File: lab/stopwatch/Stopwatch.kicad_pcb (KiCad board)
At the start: 2 copper layers, 90 x 90 mm, 8 parts, among them U1 atmega328p

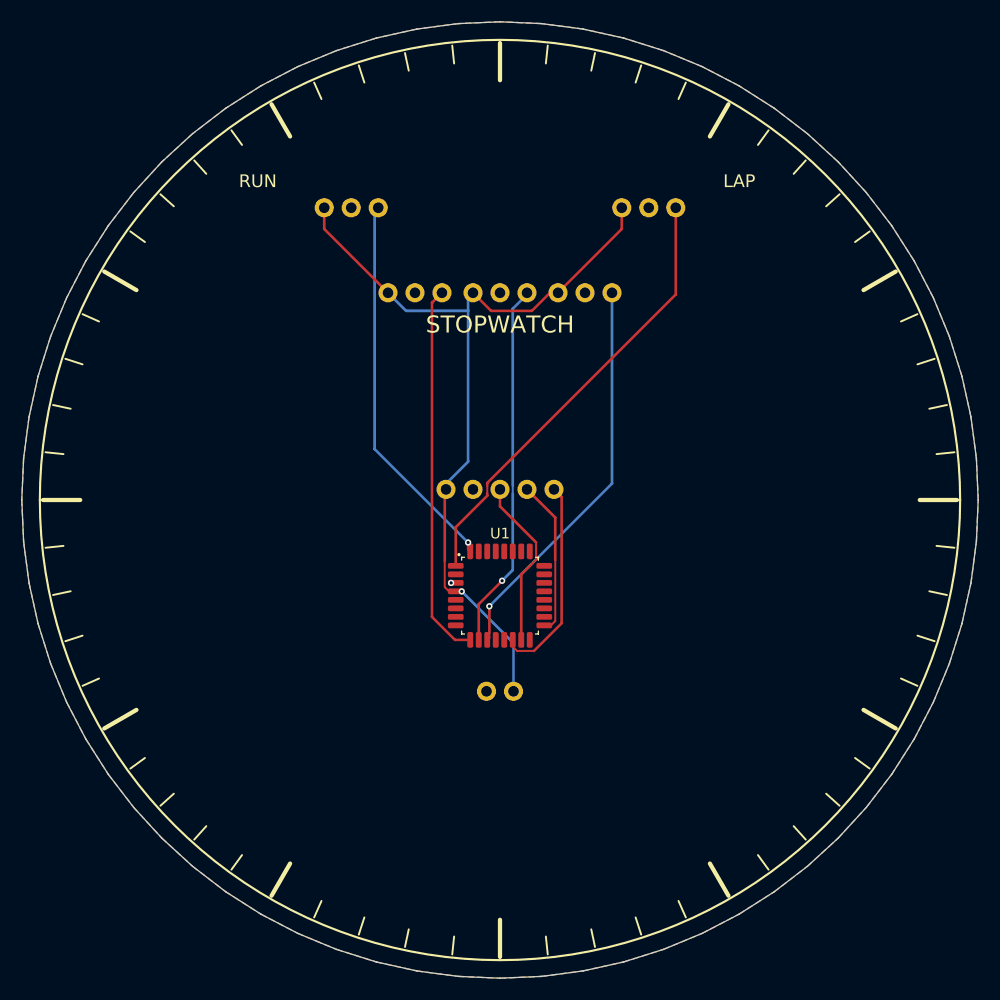
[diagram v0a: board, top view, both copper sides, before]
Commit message: lab: every board is a real board: an Arduino Nano and registry parts, routed, ready to order
The lab boards ran on simulation-only envelopes (labMcu, labDisplay, a battery). Now each is
an Arduino Nano on two sockets on the back (flashed over its USB, the image the app builds),
its lights LEDs through 1 kΩ, its knobs PTV09A pots, its display the MAX7219 eight-digit
module, its sensors an SHT31 and an SCD40 with their datasheets' support circuits, the FTDI
header for the serial console; the servo boards take 5 V on a screw terminal with a bulk
capacitor. All ten check complete with no errors or warnings, their firmware unchanged
(serial-device now on the 328P), and run in the lab without a fault (3 s each, dev host).

The registry: every interactive board must be ready to order and flash (publish.mjs refuses
one that is not; status simulation-only removed).

Claude-Session: https://claude.ai/code/session_01ATmMmxyrWxFwR3nTdXUrcx
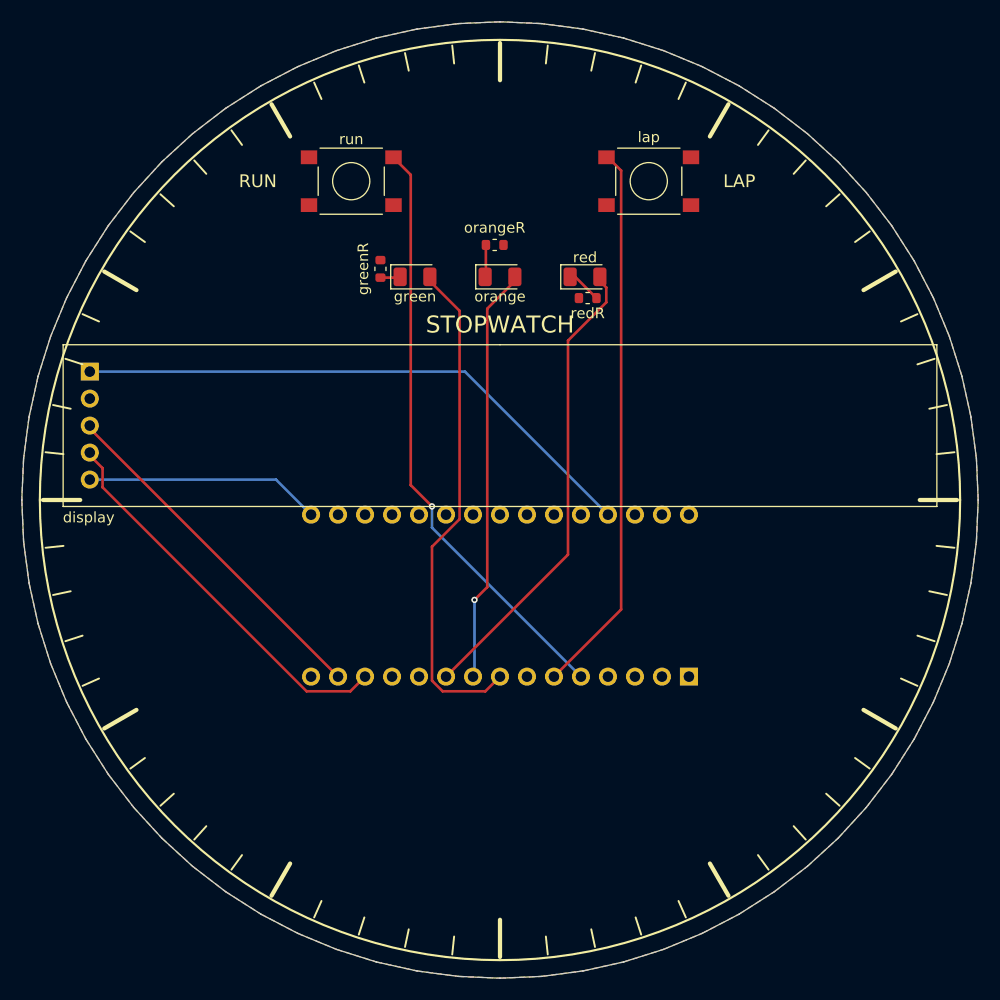
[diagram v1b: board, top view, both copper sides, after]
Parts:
- removed battery: battery, Regulated battery module
- removed the display at (145.0, 148.0)
- removed the green at (137.0, 134.0)
- removed the lap at (159.0, 125.0)
- removed the orange at (145.0, 134.0)
- removed the red at (153.0, 134.0)
- removed the run at (131.0, 125.0)
- added display: MAX7219 8-digit 7-segment LED display module, MAX7219_8digit_Module_Socket_1x05_P2.54mm, F.Cu at (145.0, 148.0)
- added green: green, LED_1206_3216Metric, F.Cu at (137.0, 134.0)
- added greenR: 1kohm, R_0603_1608Metric, F.Cu at (133.8, 133.2)
- added lap: PTS645SM43SMTR92 LFS, SW_Tactile_SPST_6x6mm_SMD, F.Cu at (159.0, 125.0)
- added orange: orange, LED_1206_3216Metric, F.Cu at (145.0, 134.0)
- added orangeR: 1kohm, R_0603_1608Metric, F.Cu at (144.5, 131.0)
- added red: red, LED_1206_3216Metric, F.Cu at (153.0, 134.0)
- added redR: 1kohm, R_0603_1608Metric, F.Cu at (153.2, 136.0)
- added run: PTS645SM43SMTR92 LFS, SW_Tactile_SPST_6x6mm_SMD, F.Cu at (131.0, 125.0)
- U1: value atmega328p -> A000005; footprint TQFP-32_7x7mm_P0.8mm -> Arduino_Nano_Socket_2x15_P2.54mm_W15.24mm; moved to B.Cu
- turned U1 to 90 degrees
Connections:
- U1 pad 1: LAP -> (no net)
- U1 pad 10: ORANGE -> RED
- U1 pad 11: RED -> (no net)
- U1 pad 13: (no net) -> LOAD
- U1 pad 14: LOAD -> MOSI
- U1 pad 15: MOSI -> (no net)
- U1 pad 16: (no net) -> SCK
- U1 pad 17: SCK -> (no net)
- U1 pad 27: (no net) -> V5
- U1 pad 29: (no net) -> GND
- U1 pad 3: GND -> (no net)
- U1 pad 4: V5 -> GND
- U1 pad 5: (no net) -> RUN
- U1 pad 6: (no net) -> LAP
- U1 pad 8: (no net) -> GREEN
- U1 pad 9: GREEN -> ORANGE
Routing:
- net V5: track 78.2 -> 54.3 mm, vias 1 -> 0
- net RUN: track 36.2 -> 56.2 mm
- net LOAD: track 19.4 -> 37.0 mm
- net MOSI: track 16.2 -> 33.3 mm
- net GREEN: track 35.4 -> 47.6 mm
- net LAP: track 42.3 -> 52.1 mm
- net SCK: track 14.7 -> 22.2 mm
- net RED: track 37.5 -> 44.1 mm, vias 1 -> 0
- net ORANGE: track 34.5 -> 39.3 mm
- net RED_K: track 0.00 -> 3.30 mm
- net ORANGE_K: track 0.00 -> 3.03 mm
- net GREEN_K: track 0.00 -> 2.09 mm
- net GND: vias 1 -> 0

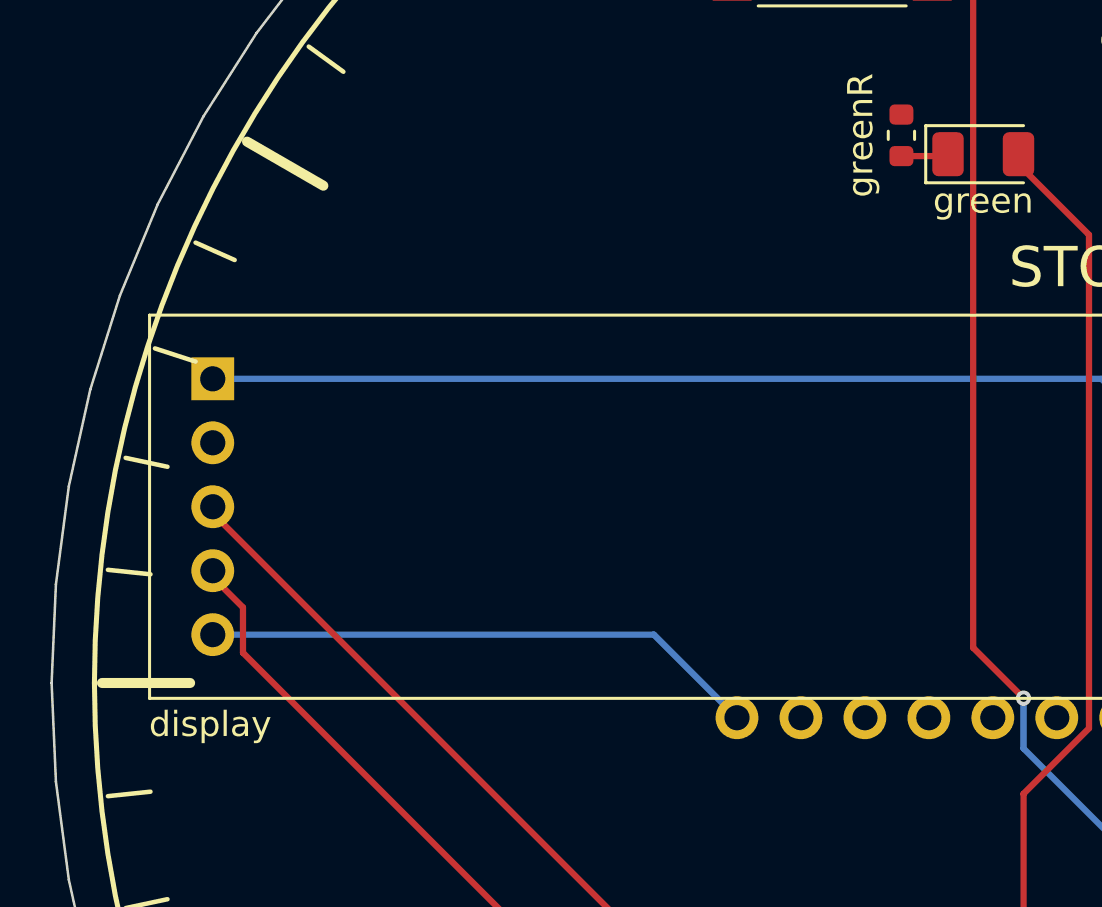
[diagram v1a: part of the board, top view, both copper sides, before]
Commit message: lab, examples, esp32-p4-touch-lcd-7b: the sweep's errors and stale parts
- lab/stopwatch: the display module stands on its socket above the Nano's socket pins. It now has
  the courtyard waiver the other Nano boards have (13 pth-inside-courtyard -> 0).
- lab/servo-controller: outline 90 x 80 -> 70 x 70 mm, with the parts where they were
  (board-oversized, plan-size: 11 % parts). Complete, 0 warnings.
- examples/blinker, examples/led-bar, devices/esp32-p4-touch-lcd-7b: `pcbkit parts` chose again
  where the recorded part no longer met the need (part-stale).

Claude-Session: https://claude.ai/code/session_01B3VRfBCg9vAvGVWujVGarr
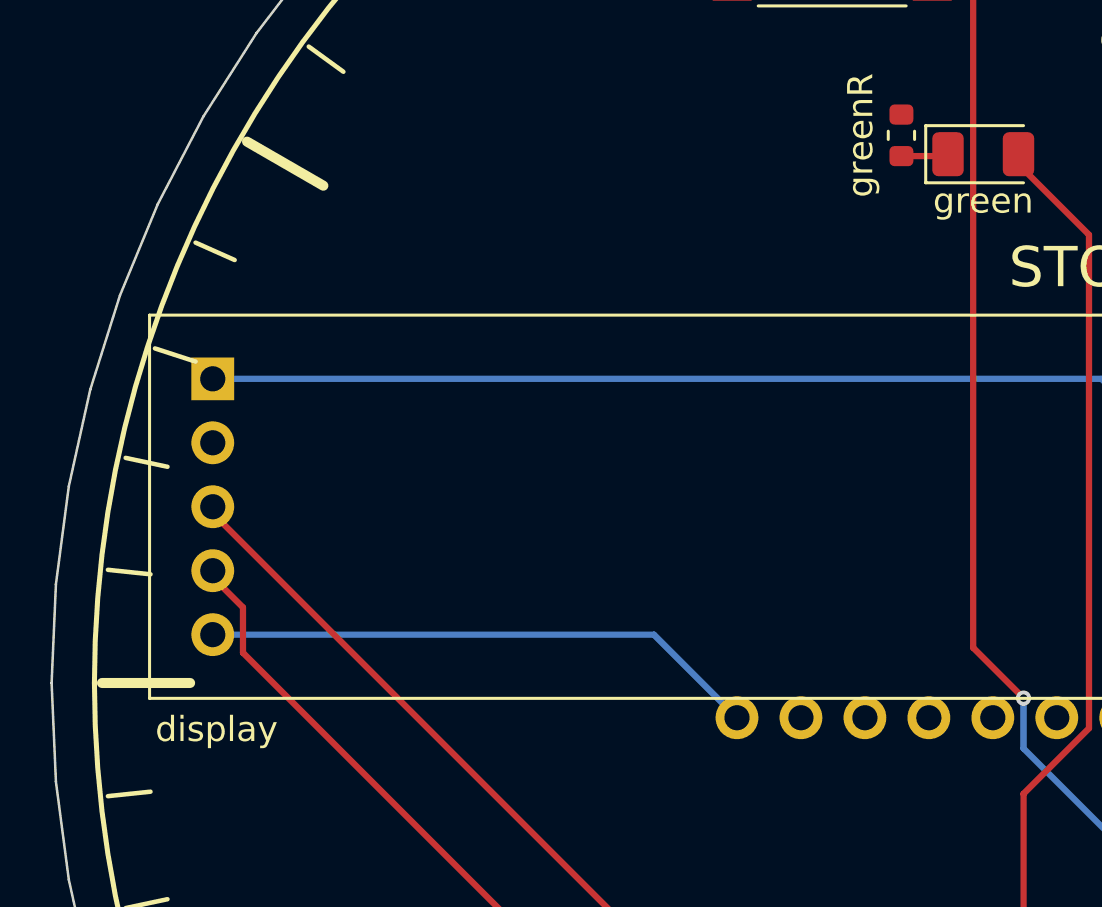
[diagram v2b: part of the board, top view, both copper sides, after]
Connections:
- lap pad 2: LAP -> GND
- run pad 2: RUN -> GND

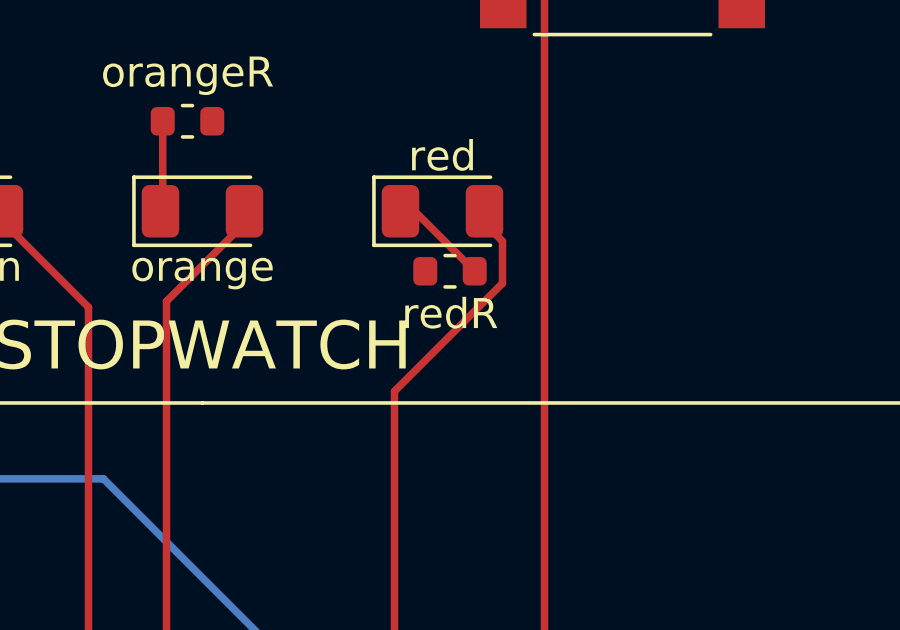
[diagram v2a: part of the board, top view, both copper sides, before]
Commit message: registry: every board rebuilt with pcbkit main 4684674e6 - the bought part named on the board
pcbkit dc07fdfd6 writes the bought row's MPN and Manufacturer (the design's own kept as DesignMPN /
DesignManufacturer) and the build chooses parts before it places (6361ec104). Each of the 44 boards
was rebuilt (; the two P4 boards  only: their builds reroute pairs):
copper unchanged on all 44 (segments, arcs and vias counted before and after), placement kept; the
Arduino and lab boards now carry the parts the catalogue gives them. The check gains only the new
judgements: part-maker (a part bought from another maker) and part-missing on hand-fitted modules
(DS1 sockets); p4-touch-7 loses part-stale. The P4 boards keep their hole-clearance errors (a
reroute is Team 3's).

Claude-Session: https://claude.ai/code/session_01BAgp959tApA8aEg85EYgfb
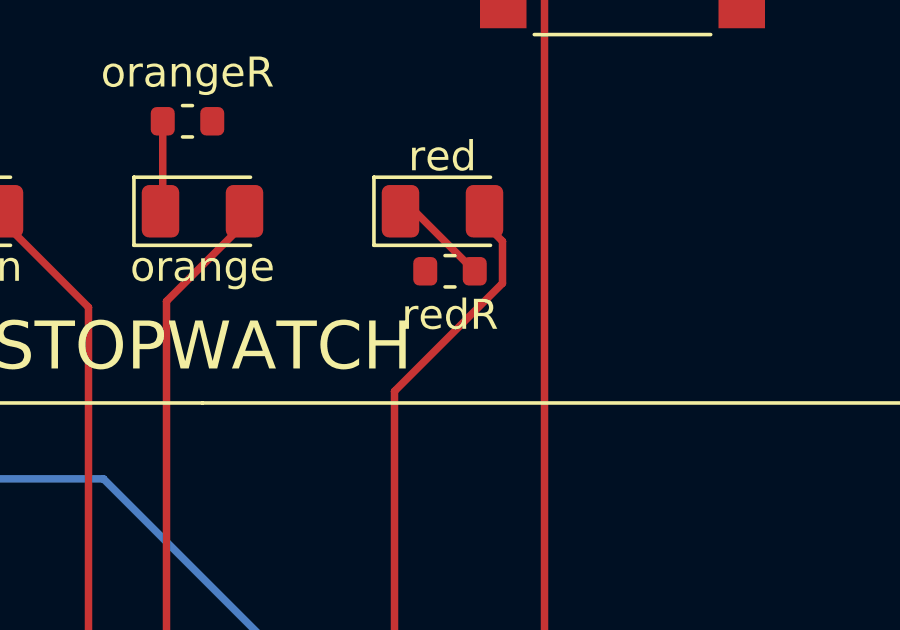
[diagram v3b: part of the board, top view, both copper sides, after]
